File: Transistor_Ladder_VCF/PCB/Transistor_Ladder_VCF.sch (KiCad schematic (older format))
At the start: 126 parts, among them J1 Audio-Jack-2_Switch, J2 Audio-Jack-2_Switch, J3 Audio-Jack-2_Switch, J4 Audio-Jack-2_Switch, J5 Audio-Jack-2_Switch, J6 Audio-Jack-2_Switch, J7 Audio-Jack-2_Switch, J8 Conn_02x05_Odd_Even, Q1 BCM847BS,135, Q2 BCM847BS,135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

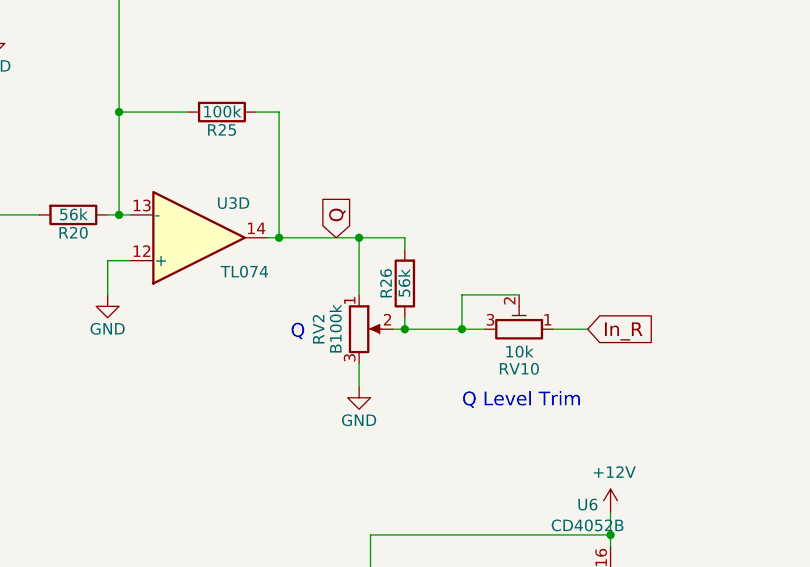
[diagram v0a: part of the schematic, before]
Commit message: Updated some resistor values
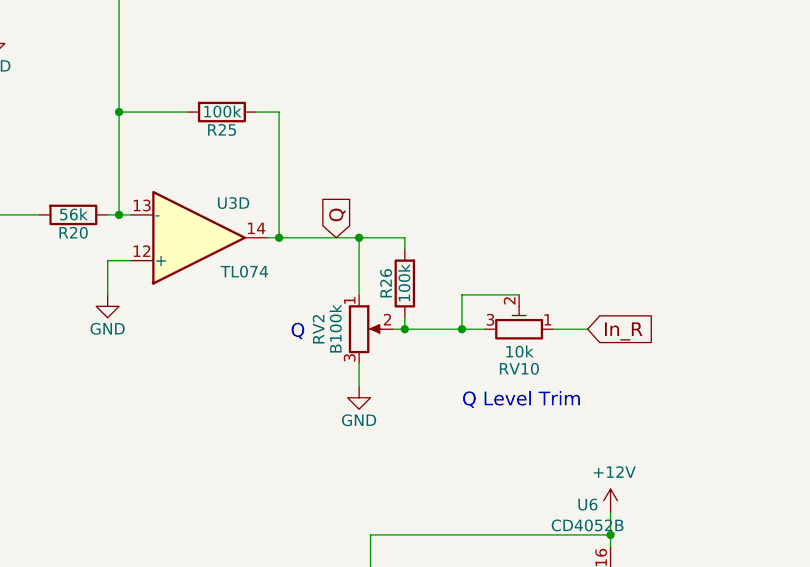
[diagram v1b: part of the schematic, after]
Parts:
- R26: value 56k -> 100k
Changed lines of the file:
@@
 P 11600 9550
 F 0 "R26" V 11680 9550 50  0000 C CNN
-F 1 "56k" V 11600 9550 50  0000 C CNN
+F 1 "100k" V 11600 9550 50  0000 C CNN
 F 2 "Resistor_SMD:R_0603_1608Metric_Pad0.98x0.95mm_HandSolder" V 11530 9550 50  0001 C CNN
 F 3 "" H 11600 9550 50  0001 C CNN
